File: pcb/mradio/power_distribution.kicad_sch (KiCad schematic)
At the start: 1 part, among them J1 2125280201

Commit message: Buck footprint updates
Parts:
- renumbered J1 to J201
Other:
- removed sheet 5V_LDO
- sheet 2v2_Buck: file 5v5_Buck.kicad_sch -> 2v2_Buck.kicad_sch
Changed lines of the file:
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@@
 		(dnp no)
 		(fields_autoplaced yes)
-		(property "Reference" "#PWR0108"
+		(property "Reference" "#PWR0202"
 			(at 153.67 39.37 0)
 			(hide yes)
@@
 			(project "mradio"
 				(path "/2cc0edad-946a-464e-a48b-49648a6334ed"
-					(reference "#PWR0108")
+					(reference "#PWR0202")
 					(unit 1)
 				)
@@
 		(dnp no)
 		(fields_autoplaced yes)
-		(property "Reference" "J1"
+		(property "Reference" "J201"
 			(at 151.13 16.5099 90)
 			(show_name no)
@@
 			(project "mradio"
 				(path "/2cc0edad-946a-464e-a48b-49648a6334ed"
-					(reference "J1")
+					(reference "J201")
 					(unit 1)
 				)
@@
 		(dnp no)
 		(fields_autoplaced yes)
-		(property "Reference" "#PWR0309"
+		(property "Reference" "#PWR0201"
 			(at 148.59 39.37 0)
 			(hide yes)
@@
 			(project "mradio"
 				(path "/2cc0edad-946a-464e-a48b-49648a6334ed"
-					(reference "#PWR0309")
+					(reference "#PWR0201")
 					(unit 1)
 				)
@@
 					(reference "#PWR0309")
 					(unit 1)
-				)
-			)
-		)
-	)
-	(sheet
-		(at 57.15 59.69)
-		(size 12.7 3.81)
-		(exclude_from_sim no)
-		(in_bom yes)
-		(on_board yes)
-		(dnp no)
-		(fields_autoplaced yes)
-		(stroke
-			(width 0.1524)
-			(type solid)
-		)
-		(fill
-			(color 0 0 0 0)
-		)
-		(property "Sheetname" "5V_LDO"
-			(at 57.15 58.9784 0)
-			(show_name no)
-			(do_not_autoplace no)
-			(effects
-				(font
-					(size 1.27 1.27)
-				)
-				(justify left bottom)
-			)
-		)
-		(property "Sheetfile" "5V_LDO.kicad_sch"
-			(at 57.15 64.0846 0)
-			(show_name no)
-			(do_not_autoplace no)
-			(effects
-				(font
-					(size 1.27 1.27)
-				)
-				(justify left top)
-			)
-		)
-		(instances
-			(project "power_distribution"
-				(path "/e6698048-9125-4cf3-9b80-868e7e50deb6"
-					(page "5")
-				)
-			)
-			(project "mradio"
-				(path "/2cc0edad-946a-464e-a48b-49648a6334ed"
-					(page "9")
 				)
 			)
@@
 			)
 		)
-		(property "Sheetfile" "5v5_Buck.kicad_sch"
+		(property "Sheetfile" "2v2_Buck.kicad_sch"
 			(at 57.15 43.7646 0)
 			(show_name no)

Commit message: Input connector
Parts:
- removed J201: 2125280201, CONN_2125280000_02_MOL, symbol symbols:2125280201
- added J202: Conn_01x02, Package_DFN_QFN:QFN-20-1EP_5x5mm_P0.65mm_EP3.35x3.35mm, symbol Connector_Generic:Conn_01x02
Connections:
- net +12V: now also J202.1 (Pin_1)
- net GND: now also J202.2 (Pin_2)
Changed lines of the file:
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@@
 	(wire
 		(pts
-			(xy 144.78 26.67) (xy 144.78 39.37)
+			(xy 120.65 22.86) (xy 120.65 29.21)
 		)
 		(stroke
@@
 	(wire
 		(pts
-			(xy 147.32 26.67) (xy 147.32 39.37)
+			(xy 118.11 22.86) (xy 118.11 29.21)
 		)
 		(stroke
@@
 	)
 	(symbol
+		(lib_id "power:+12V")
+		(at 118.11 29.21 90)
+		(unit 1)
+		(body_style 1)
+		(exclude_from_sim no)
+		(in_bom yes)
+		(on_board yes)
+		(in_pos_files yes)
+		(dnp no)
+		(fields_autoplaced yes)
+		(property "Reference" "#PWR0201"
+			(at 121.92 29.21 0)
+			(hide yes)
+			(show_name no)
+			(do_not_autoplace no)
+			(effects
+				(font
+					(size 1.27 1.27)
+				)
+			)
+		)
+		(property "Value" "+12V"
+			(at 116.84 26.67 90)
+			(show_name no)
+			(do_not_autoplace no)
+			(effects
+				(font
+					(size 1.27 1.27)
+				)
+			)
+		)
+		(property "Footprint" ""
+			(at 118.11 29.21 0)
+			(hide yes)
+			(show_name no)
+			(do_not_autoplace no)
+			(effects
+				(font
+					(size 1.27 1.27)
+				)
+			)
+		)
+		(property "Datasheet" ""
+			(at 118.11 29.21 0)
+			(hide yes)
+			(show_name no)
+			(do_not_autoplace no)
+			(effects
+				(font
+					(size 1.27 1.27)
+				)
+			)
+		)
+		(property "Description" "Power symbol creates a global label with name \"+12V\""
+			(at 118.11 29.21 0)
+			(hide yes)
+			(show_name no)
+			(do_not_autoplace no)
+			(effects
+				(font
+					(size 1.27 1.27)
+				)
+			)
+		)
+		(pin "1"
+		)
+		(instances
+			(project "mradio"
+				(path "/2cc0edad-946a-464e-a48b-49648a6334ed"
+					(reference "#PWR0201")
+					(unit 1)
+				)
+			)
+		)
+	)
+	(symbol
 		(lib_id "power:GND")
-		(at 147.32 39.37 90)
+		(at 120.65 29.21 90)
 		(unit 1)
 		(body_style 1)
@@
 		(fields_autoplaced yes)
 		(property "Reference" "#PWR0202"
-			(at 153.67 39.37 0)
+			(at 127 29.21 0)
 			(hide yes)
 			(show_name no)
@@
 		)
 		(property "Value" "GND"
-			(at 151.13 39.3699 90)
+			(at 124.46 29.2099 90)
 			(show_name no)
 			(do_not_autoplace no)
@@
 		)
 		(property "Footprint" ""
-			(at 147.32 39.37 0)
+			(at 120.65 29.21 0)
 			(hide yes)
 			(show_name no)
@@
 		)
 		(property "Datasheet" ""
-			(at 147.32 39.37 0)
+			(at 120.65 29.21 0)
 			(hide yes)
 			(show_name no)
@@
 		)
 		(property "Description" "Power symbol creates a global label with name \"GND\" , ground"
-			(at 147.32 39.37 0)
+			(at 120.65 29.21 0)
 			(hide yes)
 			(show_name no)
@@
 				)
 			)
-			(project "power_distribution"
-				(path "/e6698048-9125-4cf3-9b80-868e7e50deb6"
-					(reference "#PWR0108")
-					(unit 1)
-				)
-			)
 		)
 	)
 	(symbol
-		(lib_id "symbols:2125280201")
-		(at 144.78 26.67 90)
+		(lib_id "Connector_Generic:Conn_01x02")
+		(at 118.11 17.78 90)
 		(unit 1)
 		(body_style 1)
@@
 		(dnp no)
 		(fields_autoplaced yes)
-		(property "Reference" "J201"
-			(at 151.13 16.5099 90)
-			(show_name no)
-			(do_not_autoplace no)
-			(effects
-				(font
-					(size 1.524 1.524)
+		(property "Reference" "J202"
+			(at 123.19 16.5099 90)
+			(show_name no)
+			(do_not_autoplace no)
+			(effects
+				(font
+					(size 1.27 1.27)
 				)
 				(justify right)
 			)
 		)
-		(property "Value" "2125280201"
-			(at 151.13 19.0499 90)
-			(show_name no)
-			(do_not_autoplace no)
-			(effects
-				(font
-					(size 1.524 1.524)
+		(property "Value" "Conn_01x02"
+			(at 123.19 19.0499 90)
+			(show_name no)
+			(do_not_autoplace no)
+			(effects
+				(font
+					(size 1.27 1.27)
 				)
 				(justify right)
 			)
 		)
-		(property "Footprint" "CONN_2125280000_02_MOL"
-			(at 144.78 26.67 0)
-			(hide yes)
-			(show_name no)
-			(do_not_autoplace no)
-			(effects
-				(font
-					(size 1.27 1.27)
-					(italic yes)
-				)
-			)
-		)
-		(property "Datasheet" "https://www.molex.com/en-us/products/part-detail-pdf/2125280201?display=pdf"
-			(at 144.78 26.67 0)
-			(hide yes)
-			(show_name no)
-			(do_not_autoplace no)
-			(effects
-				(font
-					(size 1.27 1.27)
-					(italic yes)
-				)
-			)
-		)
-		(property "Description" ""
-			(at 144.78 26.67 0)
-			(hide yes)
-			(show_name no)
-			(do_not_autoplace no)
-			(effects
-				(font
-					(size 1.27 1.27)
-				)
-			)
+		(property "Footprint" "Package_DFN_QFN:QFN-20-1EP_5x5mm_P0.65mm_EP3.35x3.35mm"
+			(at 118.11 17.78 0)
+			(hide yes)
+			(show_name no)
+			(do_not_autoplace no)
+			(effects
+				(font
+					(size 1.27 1.27)
+				)
+			)
+		)
+		(property "Datasheet" ""
+			(at 118.11 17.78 0)
+			(hide yes)
+			(show_name no)
+			(do_not_autoplace no)
+			(effects
+				(font
+					(size 1.27 1.27)
+				)
+			)
+		)
+		(property "Description" "Generic connector, single row, 01x02, script generated (kicad-library-utils/schlib/autogen/connector/)"
+			(at 118.11 17.78 0)
+			(hide yes)
+			(show_name no)
+			(do_not_autoplace no)
+			(effects
+				(font
+					(size 1.27 1.27)
+				)
+			)
+		)
+		(pin "1"
 		)
 		(pin "2"
-		)
-		(pin "1"
 		)
 		(instances
 			(project "mradio"
 				(path "/2cc0edad-946a-464e-a48b-49648a6334ed"
-					(reference "J201")
+					(reference "J202")
 					(unit 1)
 				)
-			)
-			(project "power_distribution"
-				(path "/e6698048-9125-4cf3-9b80-868e7e50deb6"
-					(reference "J1")
-					(unit 1)
-				)
-			)
-		)
-	)
-	(symbol
-		(lib_id "power:+12V")
-		(at 144.78 39.37 90)
-		(unit 1)
-		(body_style 1)
-		(exclude_from_sim no)
-		(in_bom yes)
-		(on_board yes)
-		(in_pos_files yes)
-		(dnp no)
-		(fields_autoplaced yes)
-		(property "Reference" "#PWR0201"
-			(at 148.59 39.37 0)
-			(hide yes)
-			(show_name no)
-			(do_not_autoplace no)
-			(effects
-				(font
-					(size 1.27 1.27)
-				)
-			)
-		)
-		(property "Value" "+12V"
-			(at 143.51 36.83 90)
-			(show_name no)
-			(do_not_autoplace no)
-			(effects
-				(font
-					(size 1.27 1.27)
-				)
-			)
-		)
-		(property "Footprint" ""
-			(at 144.78 39.37 0)
-			(hide yes)
-			(show_name no)
-			(do_not_autoplace no)
-			(effects
-				(font
-					(size 1.27 1.27)
-				)
-			)
-		)
-		(property "Datasheet" ""
-			(at 144.78 39.37 0)
-			(hide yes)
-			(show_name no)
-			(do_not_autoplace no)
-			(effects
-				(font
-					(size 1.27 1.27)
-				)
-			)
-		)
-		(property "Description" "Power symbol creates a global label with name \"+12V\""
-			(at 144.78 39.37 0)
-			(hide yes)
-			(show_name no)
-			(do_not_autoplace no)
-			(effects
-				(font
-					(size 1.27 1.27)
-				)
-			)
-		)
-		(pin "1"
-		)
-		(instances
-			(project "mradio"
-				(path "/2cc0edad-946a-464e-a48b-49648a6334ed"
-					(reference "#PWR0201")
-					(unit 1)
-				)
-			)
-			(project "power_distribution"
-				(path "/e6698048-9125-4cf3-9b80-868e7e50deb6"
-					(reference "#PWR0309")
-					(unit 1)
-				)

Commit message: Input connector footprint
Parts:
- J202: footprint Package_DFN_QFN:QFN-20-1EP_5x5mm_P0.65mm_EP3.35x3.35mm -> molex_conn:CONN_2125280000_02_MOL
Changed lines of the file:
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@@
 			)
 		)
-		(property "Footprint" "Package_DFN_QFN:QFN-20-1EP_5x5mm_P0.65mm_EP3.35x3.35mm"
+		(property "Footprint" "molex_conn:CONN_2125280000_02_MOL"
 			(at 118.11 17.78 0)
 			(hide yes)

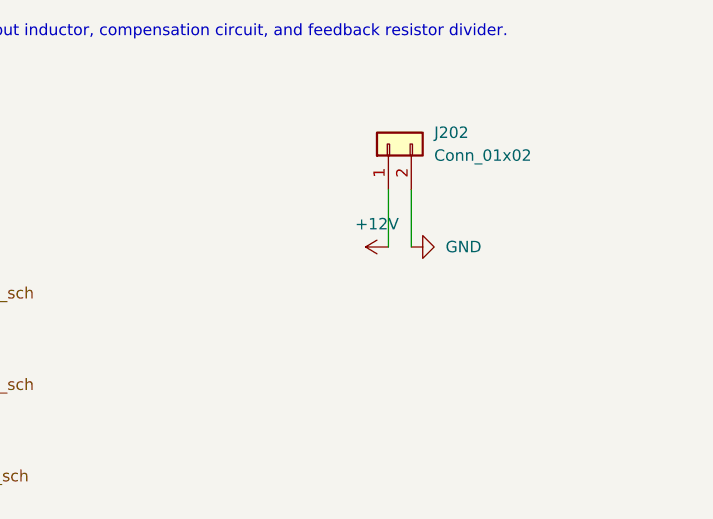
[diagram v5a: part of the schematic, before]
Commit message: Via-ed ethernet and swapped input
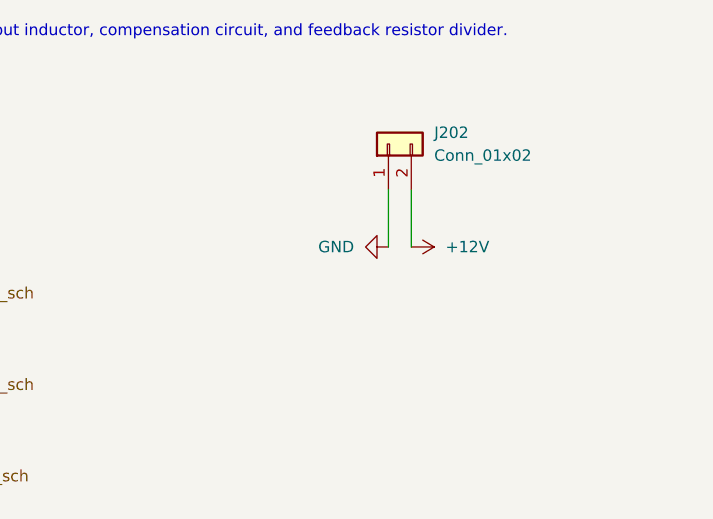
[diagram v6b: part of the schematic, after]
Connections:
- net +12V: now also J202.2 (Pin_2); no longer J202.1 (Pin_1)
- net GND: now also J202.1 (Pin_1); no longer J202.2 (Pin_2)
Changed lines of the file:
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@@
 	)
 	(symbol
-		(lib_id "power:+12V")
-		(at 118.11 29.21 90)
+		(lib_id "power:GND")
+		(at 118.11 29.21 270)
 		(unit 1)
 		(body_style 1)
@@
 		(dnp no)
 		(fields_autoplaced yes)
-		(property "Reference" "#PWR0201"
-			(at 121.92 29.21 0)
+		(property "Reference" "#PWR0202"
+			(at 111.76 29.21 0)
 			(hide yes)
 			(show_name no)
@@
 			)
 		)
-		(property "Value" "+12V"
-			(at 116.84 26.67 90)
+		(property "Value" "GND"
+			(at 114.3 29.2099 90)
 			(show_name no)
 			(do_not_autoplace no)
@@
 					(size 1.27 1.27)
 				)
+				(justify right)
 			)
 		)
@@
 			)
 		)
-		(property "Description" "Power symbol creates a global label with name \"+12V\""
+		(property "Description" "Power symbol creates a global label with name \"GND\" , ground"
 			(at 118.11 29.21 0)
 			(hide yes)
@@
 			(project "mradio"
 				(path "/2cc0edad-946a-464e-a48b-49648a6334ed"
-					(reference "#PWR0201")
+					(reference "#PWR0202")
 					(unit 1)
 				)
@@
 	)
 	(symbol
-		(lib_id "power:GND")
-		(at 120.65 29.21 90)
+		(lib_id "power:+12V")
+		(at 120.65 29.21 270)
 		(unit 1)
 		(body_style 1)
@@
 		(dnp no)
 		(fields_autoplaced yes)
-		(property "Reference" "#PWR0202"
-			(at 127 29.21 0)
+		(property "Reference" "#PWR0201"
+			(at 116.84 29.21 0)
 			(hide yes)
 			(show_name no)
@@
 			)
 		)
-		(property "Value" "GND"
+		(property "Value" "+12V"
 			(at 124.46 29.2099 90)
 			(show_name no)
@@
 					(size 1.27 1.27)
 				)
-				(justify right)
+				(justify left)
 			)
 		)
@@
 			)
 		)
-		(property "Description" "Power symbol creates a global label with name \"GND\" , ground"
+		(property "Description" "Power symbol creates a global label with name \"+12V\""
 			(at 120.65 29.21 0)
 			(hide yes)
@@
 			(project "mradio"
 				(path "/2cc0edad-946a-464e-a48b-49648a6334ed"
-					(reference "#PWR0202")
+					(reference "#PWR0201")
 					(unit 1)
 				)
